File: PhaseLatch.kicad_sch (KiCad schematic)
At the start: 120 parts, among them J1 CLK_IN, J2 NC, J3 I_IN, J4 Q_IN, J5 Databus, J6 Chip select, J7 Addressbus, J8 Signals, P1 Conn_02x10_Odd_Even, P2 Conn_02x10_Odd_Even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

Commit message: Ready for review
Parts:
- added C25, C26, C27: 100nF, Capacitor_SMD:C_0402_1005Metric, symbol Device:C_Small
- D1, D2, D3, D4, D5, D6, D7: LCSC (none) -> C2297
- R1, R3: LCSC (none) -> C25900
- R11, R12, R13, R14, R17, R18, R19, R20, R21, R22, R23, R24, R4, R5, R6, R7, R8: LCSC (none) -> C25744
- R29, R30, R31, R32, R33, R34, R35, R36, R37, R38: LCSC (none) -> C25105
- R39, R40, R41, R42, R43, R44, R45, R46: LCSC (none) -> C25077
- U1: LCSC (none) -> C3019546
- U2, U6, U7, U8: value TP74LVC1G132S5 -> SN74LVC1G132DCKR; footprint Package_TO_SOT_SMD:SOT-23-5 -> Package_TO_SOT_SMD:SOT-353_SC-70-5; LCSC (none) -> C205992
- renumbered J3 to J20, J4 to J21, J1 to J23
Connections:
- net GND: now also C25.2, C26.2, C27.2
- net VCC: now also C25.1, C26.1, C27.1

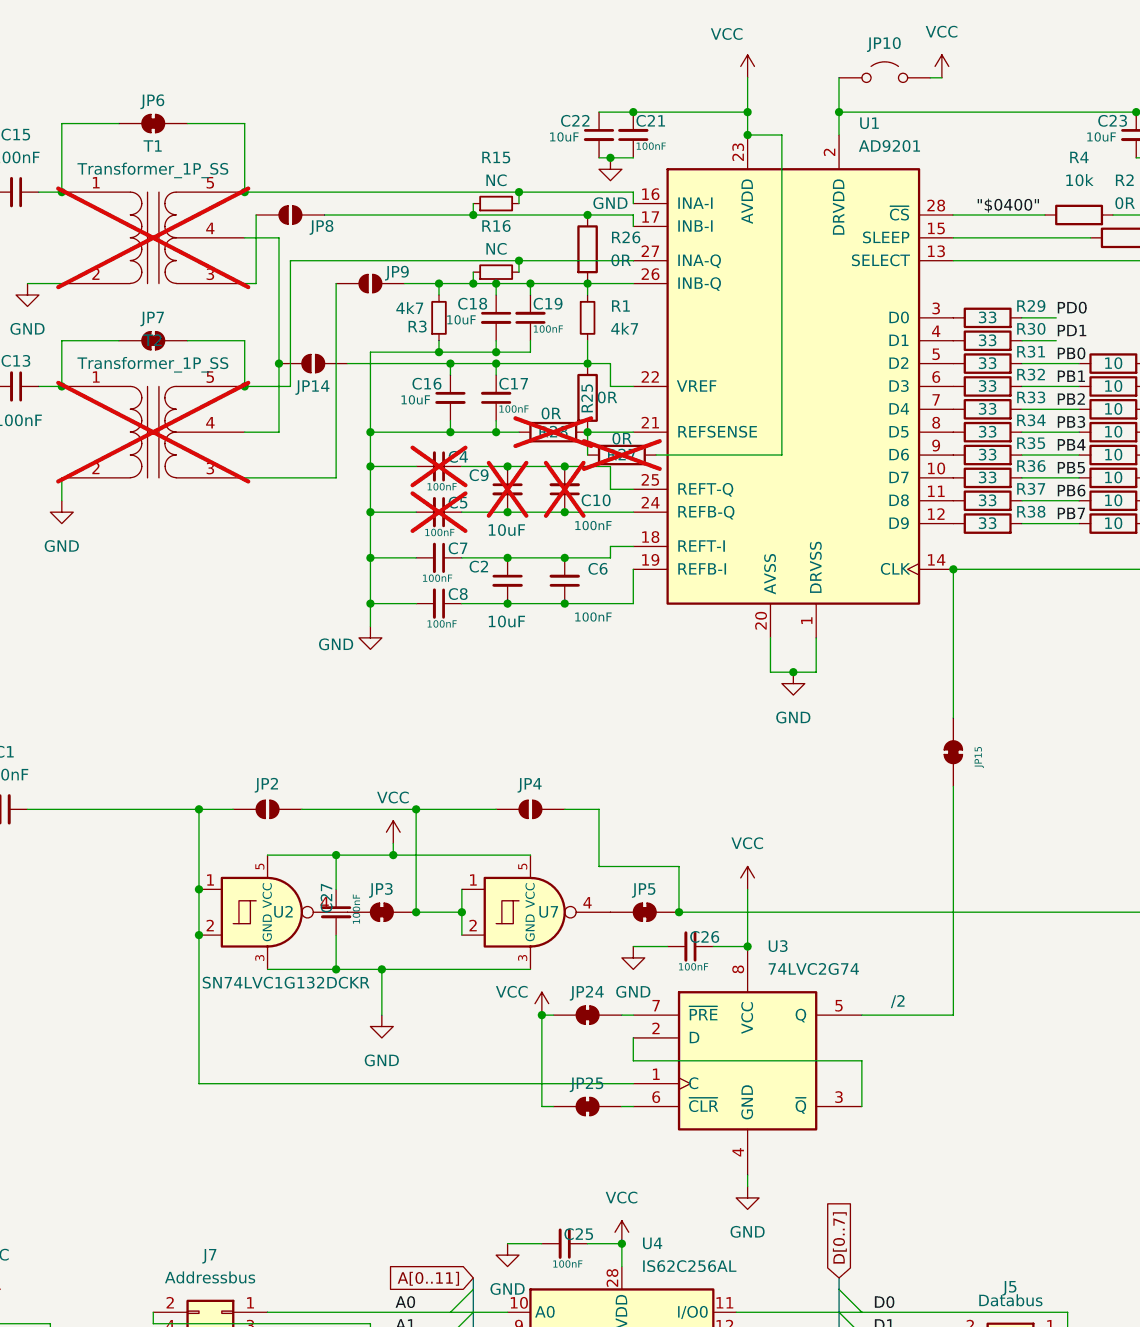
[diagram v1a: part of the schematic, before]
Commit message: Version 1.1 - correct RAM footprint
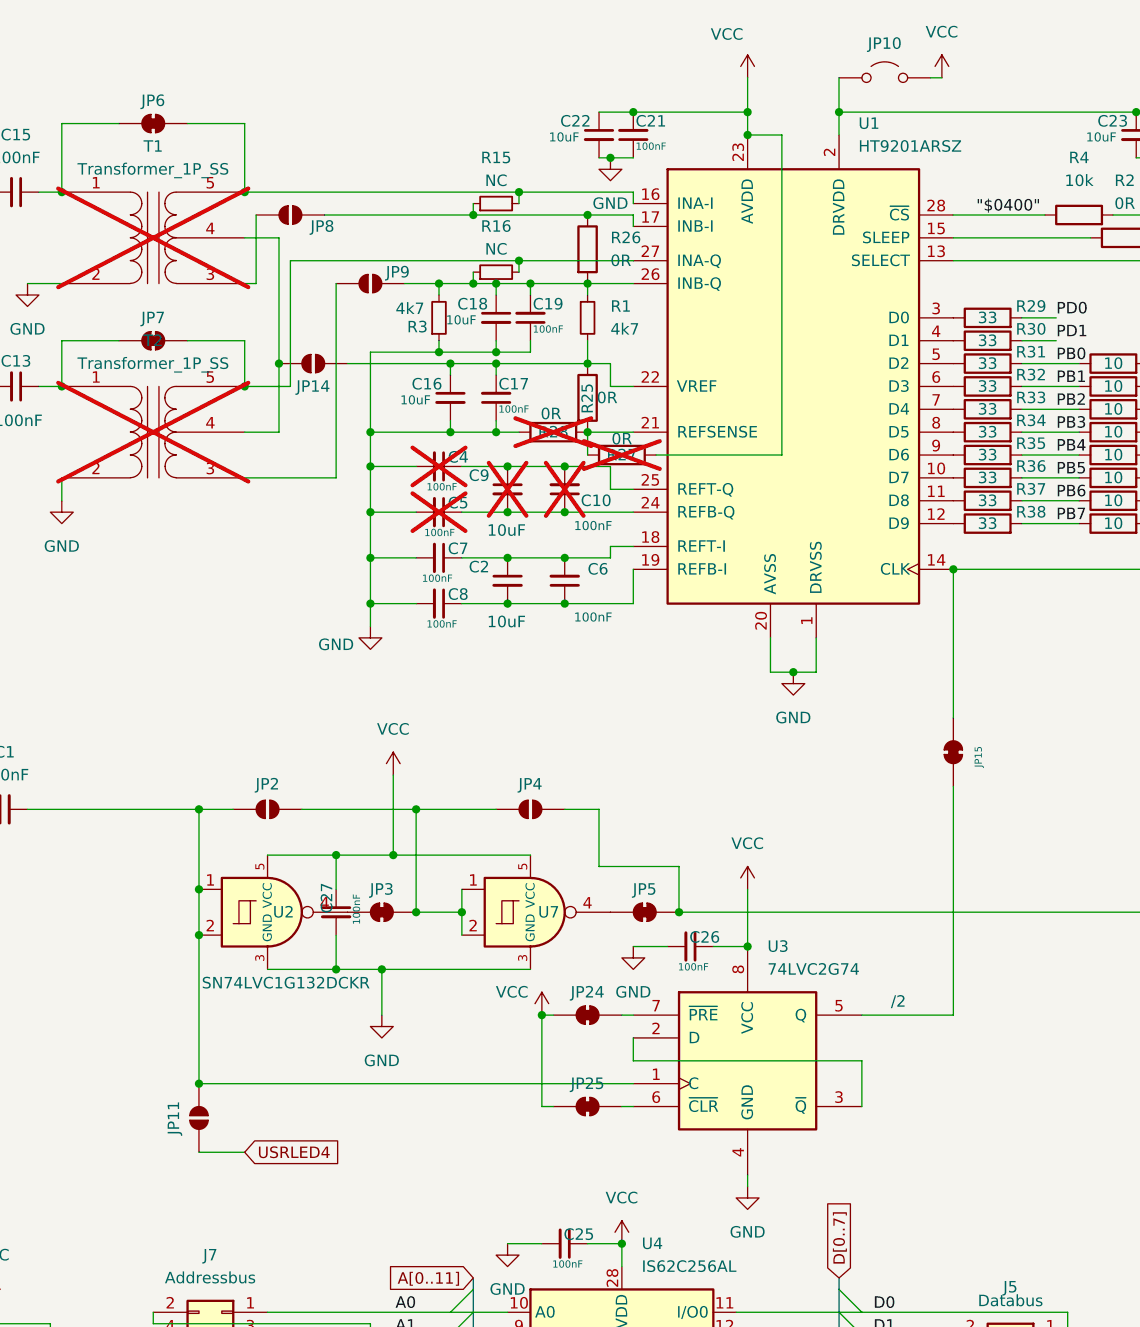
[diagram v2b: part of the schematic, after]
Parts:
- added JP11: SolderJumper_2_Open, Jumper:SolderJumper-2_P1.3mm_Open_RoundedPad1.0x1.5mm, symbol Jumper:SolderJumper_2_Open
- U1: value AD9201 -> HT9201ARSZ
- U2, U6, U7, U8: footprint Package_TO_SOT_SMD:SOT-353_SC-70-5 -> Package_TO_SOT_SMD:SOT-23-5
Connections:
- net USRLED4: now also JP11.1 (A)
- net at C1.2, JP2.1 (A), U2.1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: now also JP11.2 (B)
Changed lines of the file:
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@@
 	)
 	(junction
+		(at 53.34 130.81)
+		(diameter 0)
+		(color 0 0 0 0)
+	)
+	(junction
 		(at 27.94 173.99)
 		(diameter 0)
@@
 	(wire
 		(pts
-			(xy 74.93 104.14) (xy 74.93 105.41)
+			(xy 74.93 96.52) (xy 74.93 105.41)
 		)
 		(stroke
@@
 	(wire
 		(pts
+			(xy 53.34 138.43) (xy 58.42 138.43)
+		)
+		(stroke
+			(width 0)
+			(type default)
+		)
+	)
+	(wire
+		(pts
 			(xy 196.85 25.4) (xy 198.12 25.4)
 		)
@@
 		)
 	)
+	(global_label "USRLED4"
+		(shape input)
+		(at 58.42 138.43 0)
+		(fields_autoplaced yes)
+		(effects
+			(font
+				(size 1.27 1.27)
+			)
+			(justify left)
+		)
+		(property "Intersheetrefs" "${INTERSHEET_REFS}"
+			(at 69.8718 138.43 0)
+			(effects
+				(font
+					(size 1.27 1.27)
+				)
+				(justify left)
+				(hide yes)
+			)
+		)
+	)
 	(symbol
 		(lib_id "Connector:Conn_Coaxial_Small")
@@
 			)
 		)
-		(property "Footprint" "Package_TO_SOT_SMD:SOT-353_SC-70-5"
+		(property "Footprint" "Package_TO_SOT_SMD:SOT-23-5"
 			(at 139.954 200.152 0)
 			(effects
@@
 		(fields_autoplaced yes)
 		(property "Reference" "U1"
-			(at 126.6541 24.13 0)
+			(at 126.6033 24.13 0)
 			(effects
 				(font
@@
 			)
 		)
-		(property "Value" "AD9201"
-			(at 126.6541 26.67 0)
+		(property "Value" "HT9201ARSZ"
+			(at 126.6033 26.67 0)
 			(effects
 				(font
@@
 	)
 	(symbol
+		(lib_id "Jumper:SolderJumper_2_Open")
+		(at 53.34 134.62 90)
+		(unit 1)
+		(exclude_from_sim yes)
+		(in_bom no)
+		(on_board yes)
+		(dnp no)
+		(property "Reference" "JP11"
+			(at 50.546 134.62 0)
+			(effects
+				(font
+					(size 1.27 1.27)
+				)
+			)
+		)
+		(property "Value" "SolderJumper_2_Open"
+			(at 49.53 134.62 0)
+			(effects
+				(font
+					(size 1.27 1.27)
+				)
+				(hide yes)
+			)
+		)
+		(property "Footprint" "Jumper:SolderJumper-2_P1.3mm_Open_RoundedPad1.0x1.5mm"
+			(at 53.34 134.62 0)
+			(effects
+				(font
+					(size 1.27 1.27)
+				)
+				(hide yes)
+			)
+		)
+		(property "Datasheet" "~"
+			(at 53.34 134.62 0)
+			(effects
+				(font
+					(size 1.27 1.27)
+				)
+				(hide yes)
+			)
+		)
+		(property "Description" "Solder Jumper, 2-pole, open"
+			(at 53.34 134.62 0)
+			(effects
+				(font
+					(size 1.27 1.27)
+				)
+				(hide yes)
+			)
+		)
+		(pin "2"
+		)
+		(pin "1"
+		)
+		(instances
+			(project "PhaseLatch"
+				(path "/295f680c-5198-4d09-b94a-db6b0a3fead7"
+					(reference "JP11")
+					(unit 1)
+				)
+			)
+		)
+	)
+	(symbol
 		(lib_id "Device:C_Small")
 		(at 87.63 74.93 0)
@@
 			)
 		)
-		(property "Footprint" "Package_TO_SOT_SMD:SOT-353_SC-70-5"
+		(property "Footprint" "Package_TO_SOT_SMD:SOT-23-5"
 			(at 122.174 200.152 0)
 			(effects
@@
 			)
 		)
-		(property "Footprint" "Package_TO_SOT_SMD:SOT-353_SC-70-5"
+		(property "Footprint" "Package_TO_SOT_SMD:SOT-23-5"
 			(at 60.706 121.412 0)
 			(effects
@@
 			)
 		)
-		(property "Footprint" "Package_TO_SOT_SMD:SOT-353_SC-70-5"
+		(property "Footprint" "Package_TO_SOT_SMD:SOT-23-5"
 			(at 89.916 121.412 0)
 			(effects
@@
 	(symbol
 		(lib_id "power:VCC")
-		(at 74.93 104.14 0)
+		(at 74.93 96.52 0)
 		(unit 1)
 		(exclude_from_sim no)
@@
 		(fields_autoplaced yes)
 		(property "Reference" "#PWR04"
-			(at 74.93 107.95 0)
+			(at 74.93 100.33 0)
 			(effects
 				(font
@@
 		)
 		(property "Value" "VCC"
-			(at 74.93 99.06 0)
+			(at 74.93 91.44 0)
 			(effects
 				(font
@@
 		)
 		(property "Footprint" ""
-			(at 74.93 104.14 0)
+			(at 74.93 96.52 0)
 			(effects
 				(font
@@
 		)
 		(property "Datasheet" ""
-			(at 74.93 104.14 0)
+			(at 74.93 96.52 0)
 			(effects
 				(font
@@
 		)
 		(property "Description" "Power symbol creates a global label with name \"VCC\""
-			(at 74.93 104.14 0)
+			(at 74.93 96.52 0)
 			(effects
 				(font
